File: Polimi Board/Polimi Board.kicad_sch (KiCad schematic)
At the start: 19 parts, among them SW1 MCU Reset, SW8 SW_Push, U1 STM32F205RCTx, Y1 25MHz

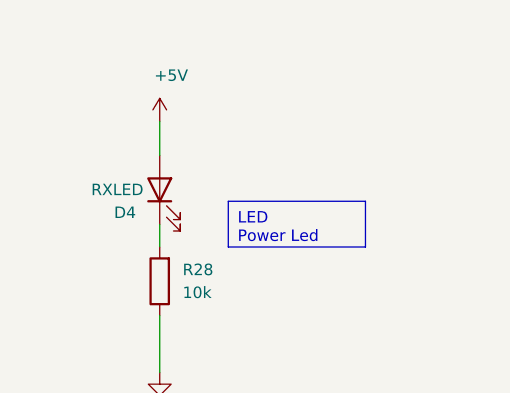
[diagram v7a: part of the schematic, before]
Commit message: adjusted some violations of ERC test
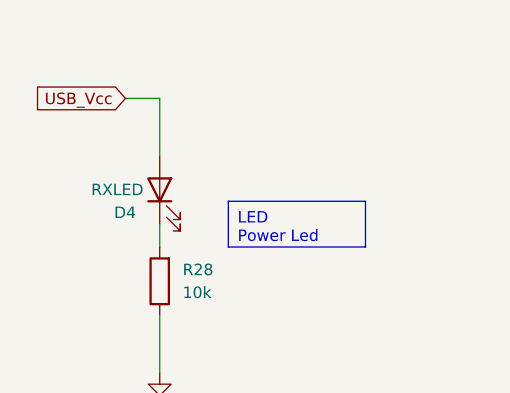
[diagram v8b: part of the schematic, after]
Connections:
- net +5V renamed USB_Vcc
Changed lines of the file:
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@@
     (stroke (width 0) (type default))
   )
-  (wire (pts (xy 34.29 30.48) (xy 34.29 34.29))
+  (wire (pts (xy 34.29 27.94) (xy 34.29 34.29))
     (stroke (width 0) (type default))
   )
@@
   )
   (wire (pts (xy 147.32 171.45) (xy 147.32 172.72))
+    (stroke (width 0) (type default))
+  )
+  (wire (pts (xy 30.48 27.94) (xy 34.29 27.94))
     (stroke (width 0) (type default))
   )
@@
   (label "USART_RTS" (at 200.66 88.9 0) (fields_autoplaced)
     (effects (font (size 1.27 1.27)) (justify left bottom))
+  )
+  (global_label "USB_Vcc" (shape input) (at 30.48 27.94 180) (fields_autoplaced)
+    (effects (font (size 1.27 1.27)) (justify right))
+    (property "Intersheetrefs" "${INTERSHEET_REFS}" (at 19.4514 27.94 0)
+      (effects (font (size 1.27 1.27)) (justify right) hide)
+    )
   )
   (symbol (lib_id "Device:C") (at 191.77 43.18 0) (unit 1)
@@
         )
       )
-    )
-  )
-  (symbol (lib_id "power:+5V") (at 34.29 30.48 0) (unit 1)
-    (in_bom yes) (on_board yes) (dnp no)
-    (property "Reference" "#PWR085" (at 34.29 34.29 0)
-      (effects (font (size 1.27 1.27)) hide)
-    )
-    (property "Value" "+5V" (at 35.56 25.4 0)
-      (effects (font (size 1.27 1.27)))
-    )
-    (property "Footprint" "" (at 34.29 30.48 0)
-      (effects (font (size 1.27 1.27)) hide)
-    )
-    (property "Datasheet" "" (at 34.29 30.48 0)
-      (effects (font (size 1.27 1.27)) hide)
-    )
-    (pin "1")
-    (instances
-      (project "Polimi Board"
-        (path "/319fe76e-1f98-44b3-99b0-af1a9ad7322c"
-          (reference "#PWR085") (unit 1)
-        )
-      )
